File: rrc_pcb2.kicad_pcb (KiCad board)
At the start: 2 copper layers, 146.1 x 72.1 mm, 16 parts, among them J1 buzzer_toggle_pin, J2 battery_header, U1 BN220-GPS, U2 INA260, U3 Teensy4.1, U4 voltReg, U5 MS5611, U6 logo

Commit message: updated rrc_pcb2 schematic and pcb files
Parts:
- removed D1: ASMB-MTB0-0A3A2, LED_4pin:LED_4PIN
- J2: footprint Connector_JST:JST_GH_SM02B-GHS-TB_1x02-1MP_P1.25mm_Horizontal -> Connector_PinSocket_2.54mm:PinSocket_1x02_P2.54mm_Vertical
- turned J2 to 180 degrees
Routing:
- net B: track 10.1 -> 0.00 mm
- net G: track 7.12 -> 0.00 mm
- net R: track 7.12 -> 0.00 mm
- net Net-(J2-Pin_1): track 19.2 -> 16.3 mm
- net Net-(J2-Pin_2): track 18.8 -> 16.1 mm

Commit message: big cleanup of files
also new teensy4.1 symbo(the accurate one now) and fixed rfd900 schematic
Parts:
- J2: footprint Connector_PinSocket_2.54mm:PinSocket_1x02_P2.54mm_Vertical -> Connector_JST:JST_GH_SM02B-GHS-TB_1x02-1MP_P1.25mm_Horizontal
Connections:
- RF1 pad +5V: VCC -> (no net)
- RF1 pad GND: GND -> (no net)
- RF1 pad SIRX: RX2 -> (no net)
- RF1 pad SITX: TX2 -> (no net)
- U3 pad 0: (no net) -> unconnected-(U3-0_RX1_CRX2_CS1-Pad0)
- U3 pad 10: TX2 -> unconnected-(U3-10_CS_MQSR-Pad10)
- U3 pad 15: T_VCC -> unconnected-(U3-15_A1_RX3_SPDIF_IN-Pad15)
- U3 pad 16: SCL2 -> SCL1
- U3 pad 17: SDA2 -> SDA1
- U3 pad 18: Net-(BZ1--) -> SDA
- U3 pad 19: Net-(J1-Pin_2) -> SCL
- U3 pad 2: unconnected-(U3-0_RX1_CRX2_CS1-Pad2) -> B
- U3 pad 20: RX7 -> unconnected-(U3-20_A6_TX5_LRCLK1-Pad20)
- U3 pad 21: TX7 -> unconnected-(U3-21_A7_RX5_BCLK1-Pad21)
- U3 pad 24: unconnected-(U3-32_OUT1B-Pad24) -> SCL2
- U3 pad 25: unconnected-(U3-33_MCLK2-Pad25) -> SDA2
- U3 pad 26: unconnected-(U3-34_RX8-Pad26) -> Net-(BZ1--)
- U3 pad 27: unconnected-(U3-35_TX8-Pad27) -> Net-(J1-Pin_2)
- U3 pad 28: unconnected-(U3-36_CS-Pad28) -> RX7
- U3 pad 29: unconnected-(U3-37_CS-Pad29) -> TX7
- U3 pad 3: unconnected-(U3-1_TX1_CTX2_MISO1-Pad3) -> G
- U3 pad 38: SCL1 -> unconnected-(U3-38_CS1_IN1-Pad38)
- U3 pad 39: SDA1 -> unconnected-(U3-39_MISO1_OUT1A-Pad39)
- U3 pad 4: B -> R
- U3 pad 40: SDA -> unconnected-(U3-40_A16-Pad40)
- U3 pad 41: SCL -> unconnected-(U3-41_A17-Pad41)
- U3 pad 49: unconnected-(U3-VUSB-Pad49) -> (no net)
- U3 pad 5: G -> unconnected-(U3-5_IN2-Pad5)
- U3 pad 6: R -> unconnected-(U3-6_OUT1D-Pad6)
- U3 pad 66: unconnected-(U3-D--Pad66) -> (no net)
- U3 pad 67: unconnected-(U3-D+-Pad67) -> (no net)
- U3 pad 7: unconnected-(U3-5_IN2-Pad7) -> RX2
- U3 pad 8: unconnected-(U3-6_OUT1D-Pad8) -> TX2
- U3 pad 9: RX2 -> unconnected-(U3-9_OUT1C-Pad9)
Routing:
- net unconnected-(U3-10_CS_MQSR-Pad10): track 0.00 -> 107.0 mm
- net TX2: track 107.0 -> 0.00 mm
- net unconnected-(U3-9_OUT1C-Pad9): track 0.00 -> 100.9 mm
- net RX2: track 100.9 -> 0.00 mm

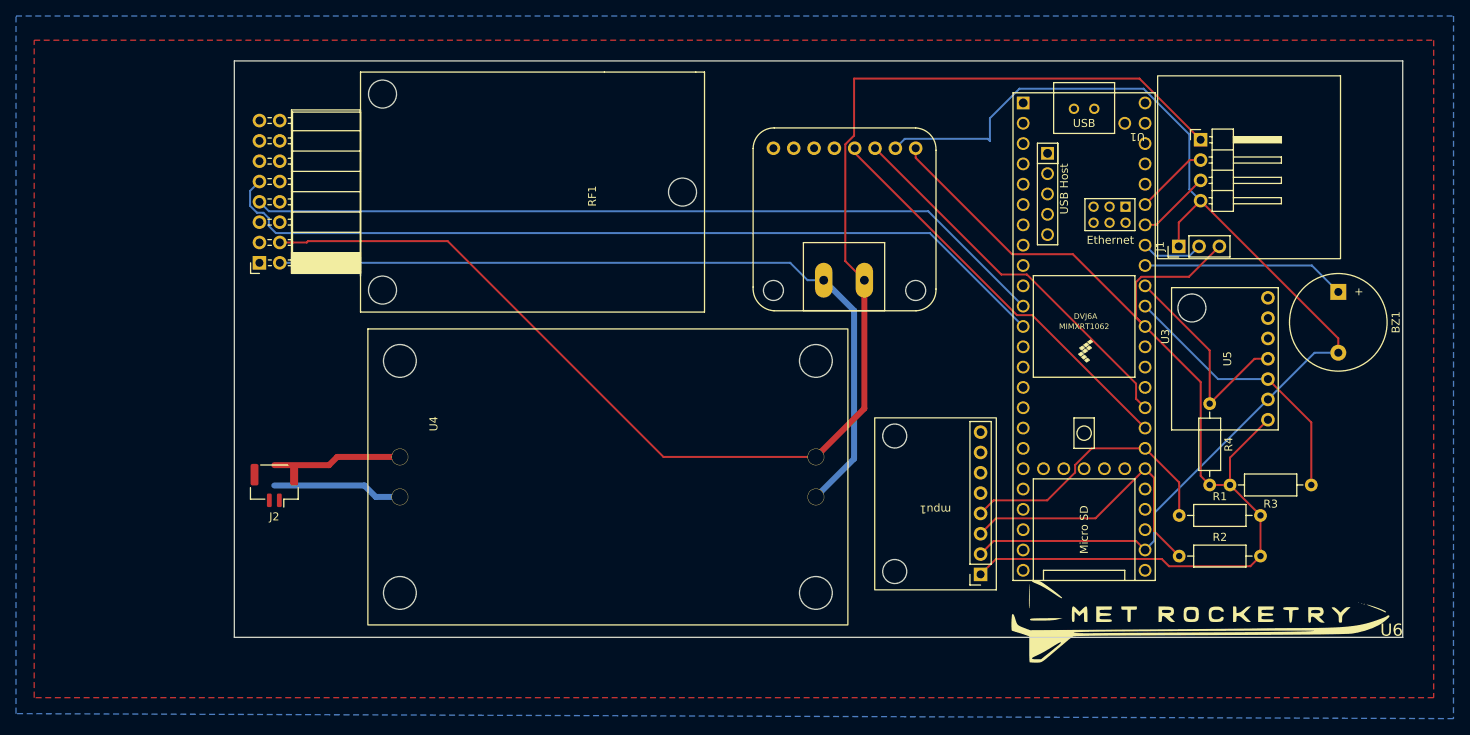
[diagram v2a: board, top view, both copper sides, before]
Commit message: fixed rfd and netlists for teensy4.1
fixed the rfd netlists and teensy pwr netlists and also fixed the pinout and wiring for rfd
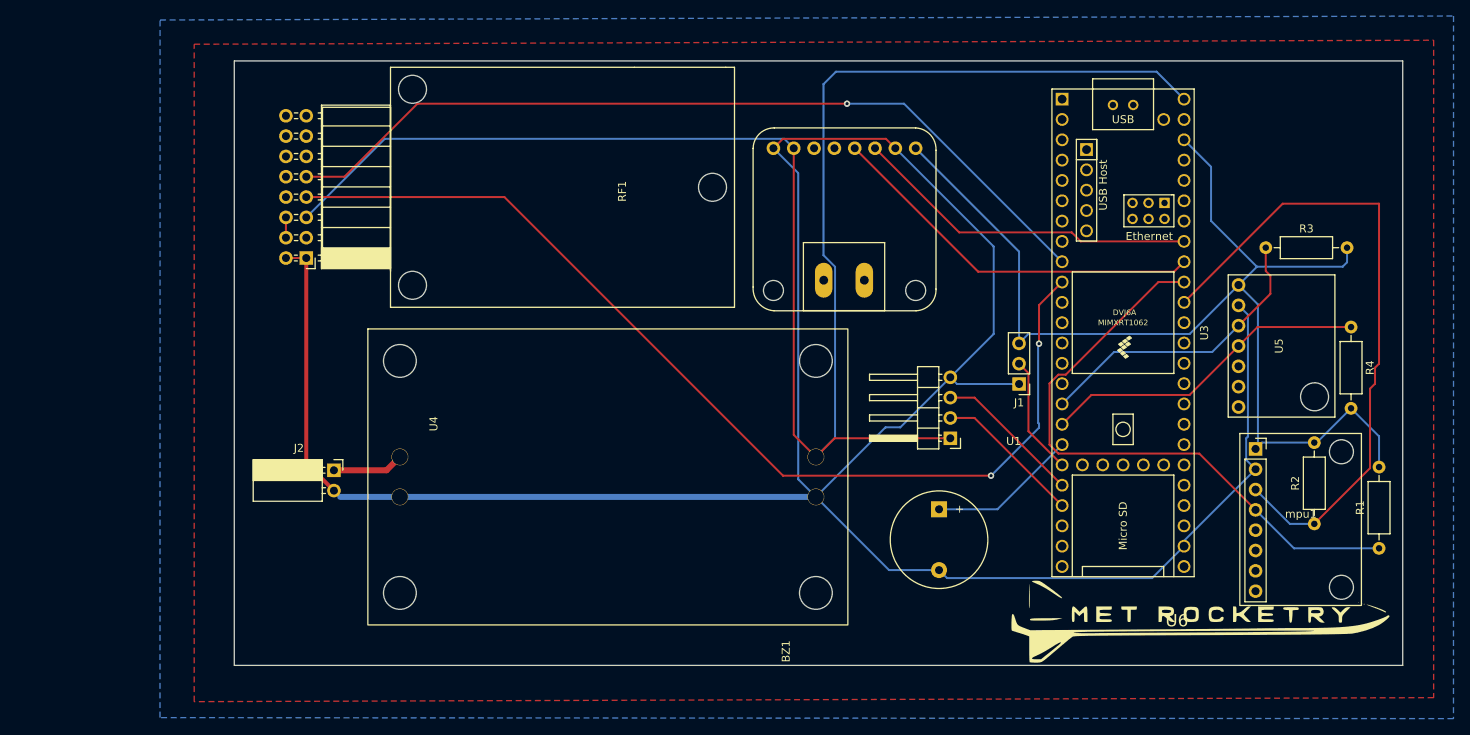
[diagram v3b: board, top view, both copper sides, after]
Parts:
- J2: footprint Connector_JST:JST_GH_SM02B-GHS-TB_1x02-1MP_P1.25mm_Horizontal -> Connector_PinSocket_2.54mm:PinSocket_1x02_P2.54mm_Horizontal
- moved U1 66.7 mm to (113.9, 53.0), turned to 0 degrees
- moved BZ1 56.8 mm to (130.0, 76.7)
- moved mpu1 45.7 mm to (175.2, 77.8), turned to 0 degrees
- moved R3 30.2 mm to (170.8, 44.0), turned to 0 degrees
- moved J1 26.4 mm to (140.0, 61.0), turned to 180 degrees
- moved R1 25.3 mm to (185.0, 81.6), turned to 90 degrees
- moved R4 20.1 mm to (181.5, 53.9)
- moved R2 17.4 mm to (176.9, 78.5), turned to 90 degrees
- moved U5 11.4 mm to (163.6, 56.3), turned to -90 degrees
- moved J2 7.69 mm to (54.4, 71.8), turned to 0 degrees
- moved U3 4.89 mm to (153.0, 54.6)
- moved RF1 3.80 mm to (61.4, 21.5)
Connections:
- BZ1 pad 2: T_GND -> GND
- J1 pad 1: T_GND -> GND
- J2 pad 2: Net-(J2-Pin_2) -> GND
- RF1 pad +5VUSB: (no net) -> VCC
- RF1 pad SIRX: (no net) -> TX2
- U1 pad 4: T_GND -> GND
- U2 pad 1: VCC -> unconnected-(U2-VIN+-Pad1)
- U2 pad 10: unconnected-(U2-IN--Pad10) -> GND
- U2 pad 2: GND -> unconnected-(U2-VIN--Pad2)
- U2 pad 4: T_GND -> GND
- U2 pad 9: unconnected-(U2-IN+-Pad9) -> VCC
- U3 pad 2: B -> unconnected-(U3-2_OUT2-Pad2)
- U3 pad 3: G -> unconnected-(U3-3_LRCLK2-Pad3)
- U3 pad 34: T_GND -> GND
- U3 pad 4: R -> unconnected-(U3-4_BCLK2-Pad4)
- U4 pad 2: Net-(J2-Pin_2) -> GND
- U5 pad 2: T_GND -> GND
- mpu1 pad 2: T_GND -> GND
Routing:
- net GND: track 99.5 -> 309.6 mm
- net T_GND: track 144.0 -> 0.00 mm
- net TX2: track 0.00 -> 128.3 mm, vias 0 -> 2
- net unconnected-(U3-10_CS_MQSR-Pad10): track 107.0 -> 0.00 mm
- net RX2: track 0.00 -> 106.4 mm, vias 0 -> 1
- net unconnected-(U3-9_OUT1C-Pad9): track 100.9 -> 0.00 mm
- net SCL1: track 36.6 -> 82.0 mm
- net VCC: track 176.0 -> 218.3 mm
- net SDA1: track 34.6 -> 76.3 mm
- net Net-(J2-Pin_2): track 16.1 -> 0.00 mm
- net SDA2: track 27.7 -> 41.2 mm
- net RX7: track 9.24 -> 18.5 mm
- net TX7: track 9.24 -> 18.5 mm
- net Net-(J2-Pin_1): track 16.3 -> 8.93 mm
- net Net-(J1-Pin_2): track 7.78 -> 14.9 mm
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- added copper zone on F.Cu, net (none)
- added copper zone on B.Cu, net GND
- removed copper zone on B.Cu, net T_GND
- removed copper zone on F.Cu, net T_VCC
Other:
- board size 146.1 x 72.1 mm -> 146.1 x 75.6 mm

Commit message: small fixes to traces
fixed pwr traces; moved them slightly away to avoid any possible bridging, also changed batt gnd to diff plate
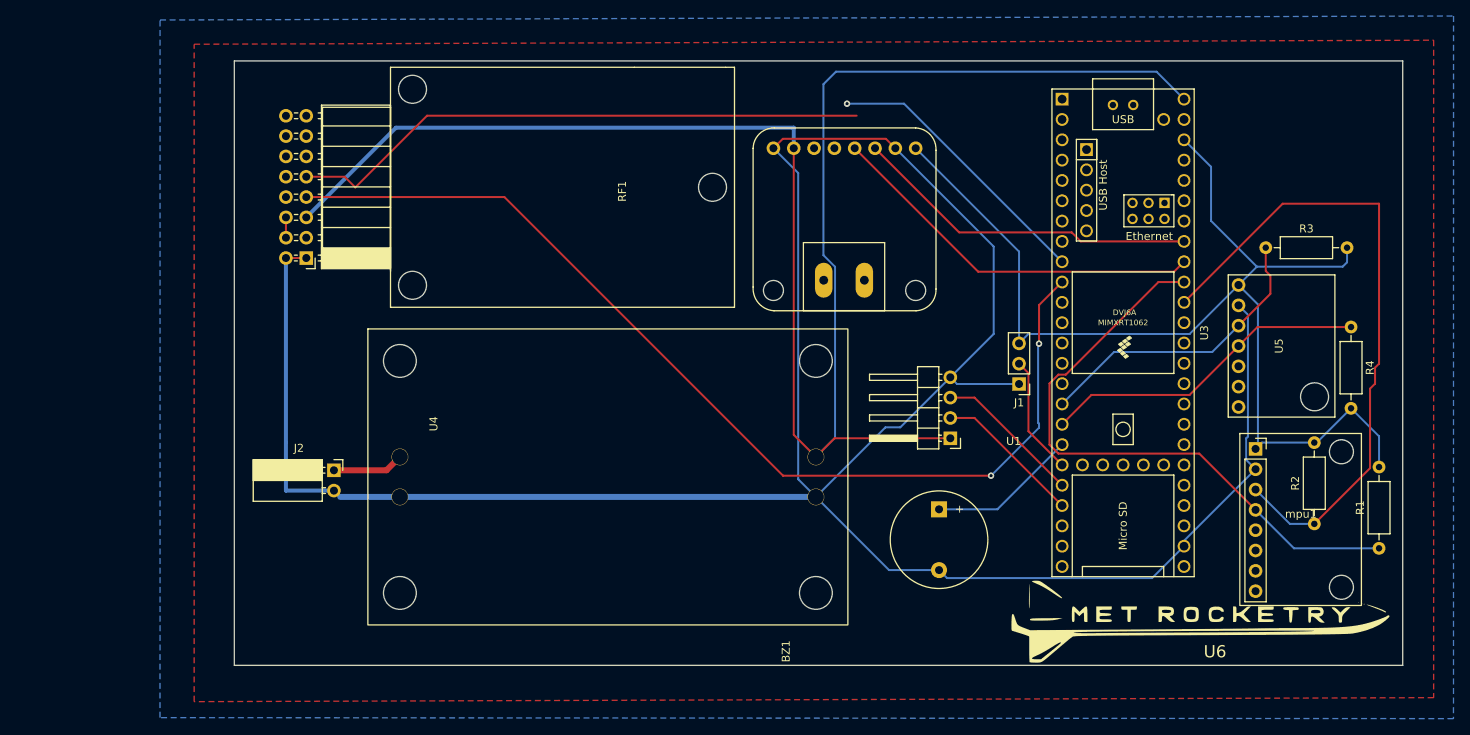
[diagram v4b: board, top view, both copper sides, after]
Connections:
- RF1 pad GND: (no net) -> GND
- U3 pad VIN: (no net) -> VCC
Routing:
- net GND: track 309.6 -> 314.2 mm
- net VCC: track 218.3 -> 221.0 mm
- net RX2: track 106.4 -> 108.1 mm
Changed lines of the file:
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@@
 			(layers "*.Cu" "*.Mask")
 			(remove_unused_layers no)
+			(net 2 "VCC")
 		)
 		(model "${KICAD_USER_DIR}/teensy.pretty/Teensy_4.1_Assembly.STEP"
@@
 		(at 159.724459 90.621103)
 		(property "Reference" "U6"
-			(at 0 0 0)
+			(at 4.775541 3.878897 0)
 			(layer "F.SilkS")
 			(effects
@@
 		(fp_arc
 			(start 11.351033 8.63642)
-			(mid 10.561541 10.466208)
+			(mid 10.56154 10.466212)
 			(end 8.709433 11.20182)
 			(stroke
@@
 			(layers "*.Cu" "*.Mask")
 			(remove_unused_layers no)
+			(net 1 "GND")
 		)
 		(pad "GND" thru_hole oval
@@
 			(layers "*.Cu" "*.Mask")
 			(remove_unused_layers no)
+			(net 1 "GND")
 		)
 		(pad "P0.1" thru_hole oval
@@
 	)
 	(segment
-		(start 50.901193 45.292707)
-		(end 50.901193 70.904861)
-		(width 0.5)
-		(layer "F.Cu")
-		(net 1)
-	)
-	(segment
 		(start 123.363834 30.392837)
 		(end 110.473834 30.392837)
@@
 	)
 	(segment
-		(start 50.901193 70.904861)
-		(end 54.360827 74.364495)
-		(width 0.5)
-		(layer "F.Cu")
-		(net 1)
-	)
-	(segment
 		(start 50.901193 45.292707)
 		(end 48.361193 45.292707)
@@
 	)
 	(segment
+		(start 48.361193 74.361193)
+		(end 48.364495 74.364495)
+		(width 0.25)
+		(layer "B.Cu")
+		(net 1)
+	)
+	(segment
 		(start 132.24857 61.04)
 		(end 131.410806 60.202236)
@@
 	)
 	(segment
+		(start 48.361193 45.292707)
+		(end 48.361193 68.364861)
+		(width 0.5)
+		(layer "B.Cu")
+		(net 1)
+	)
+	(segment
 		(start 130 84.3)
 		(end 131 85.3)
@@
 	)
 	(segment
+		(start 48.364495 74.364495)
+		(end 54.360827 74.364495)
+		(width 0.5)
+		(layer "B.Cu")
+		(net 1)
+	)
+	(segment
+		(start 48.361193 68.364861)
+		(end 48.361193 74.361193)
+		(width 0.5)
+		(layer "B.Cu")
+		(net 1)
+	)
+	(segment
 		(start 140 61.04)
 		(end 132.24857 61.04)
@@
 	)
 	(segment
-		(start 50.901193 40.212707)
-		(end 60.721063 30.392837)
-		(width 0.25)
-		(layer "B.Cu")
-		(net 2)
-	)
-	(segment
 		(start 160.62386 25.433432)
 		(end 157.190428 22)
@@
 	)
 	(segment
-		(start 110.663834 30.392837)
-		(end 111.838834 31.567837)
-		(width 0.25)
+		(start 55.80695 35.30695)
+		(end 62.1139 29)
+		(width 0.5)
 		(layer "B.Cu")
 		(net 2)
@@
 	)
 	(segment
+		(start 50.901193 40.212707)
+		(end 55.80695 35.30695)
+		(width 0.5)
+		(layer "B.Cu")
+		(net 2)
+	)
+	(segment
 		(start 157.190428 22)
 		(end 117.107668 22)
@@
 	)
 	(segment
-		(start 60.721063 30.392837)
-		(end 110.663834 30.392837)
-		(width 0.25)
+		(start 111.838834 29)
+		(end 111.838834 31.567837)
+		(width 0.5)
 		(layer "B.Cu")
 		(net 2)
@@
 	)
 	(segment
+		(start 62.1139 29)
+		(end 111.838834 29)
+		(width 0.5)
+		(layer "B.Cu")
+		(net 2)
+	)
+	(segment
 		(start 183.875 61.625)
 		(end 183.875 71.555786)
@@
 	)
 	(segment
-		(start 55.67105 35.132707)
-		(end 50.901193 35.132707)
+		(start 119.696243 27.5)
+		(end 66 27.5)
+		(width 0.25)
+		(layer "F.Cu")
+		(net 55)
+	)
+	(segment
+		(start 50.901193 35.132707)
+		(end 55.69606 35.132707)
 		(width 0.25)
 		(layer "F.Cu")
@@
 	)
 	(segment
-		(start 118.5 26)
-		(end 64.803757 26)
+		(start 55.69606 35.132707)
+		(end 57.031677 36.468324)
 		(width 0.25)
 		(layer "F.Cu")
@@
 	)
 	(segment
-		(start 64.803757 26)
-		(end 55.67105 35.132707)
+		(start 66 27.5)
+		(end 57.031677 36.468324)
 		(width 0.25)
 		(layer "F.Cu")
@@
 		(min_thickness 0.254)
 		(filled_areas_thickness no)
-		(fill
+		(fill yes
 			(thermal_gap 0.508)
 			(thermal_bridge_width 0.508)
@@
 		(min_thickness 0.254)
 		(filled_areas_thickness no)
-		(fill
+		(fill yes
 			(thermal_gap 0.508)
 			(thermal_bridge_width 0.508)

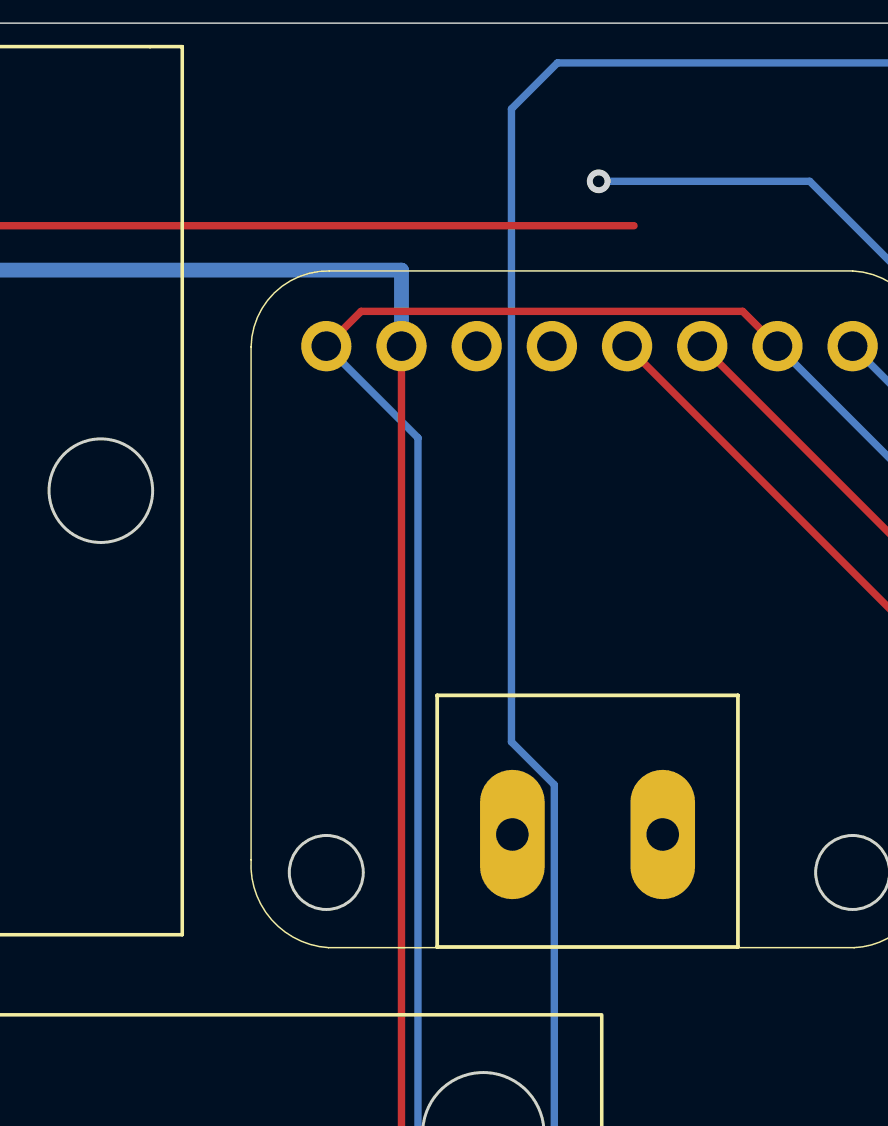
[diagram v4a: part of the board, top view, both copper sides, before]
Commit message: exported pcb to fabrication
also fixed rfd rx trace
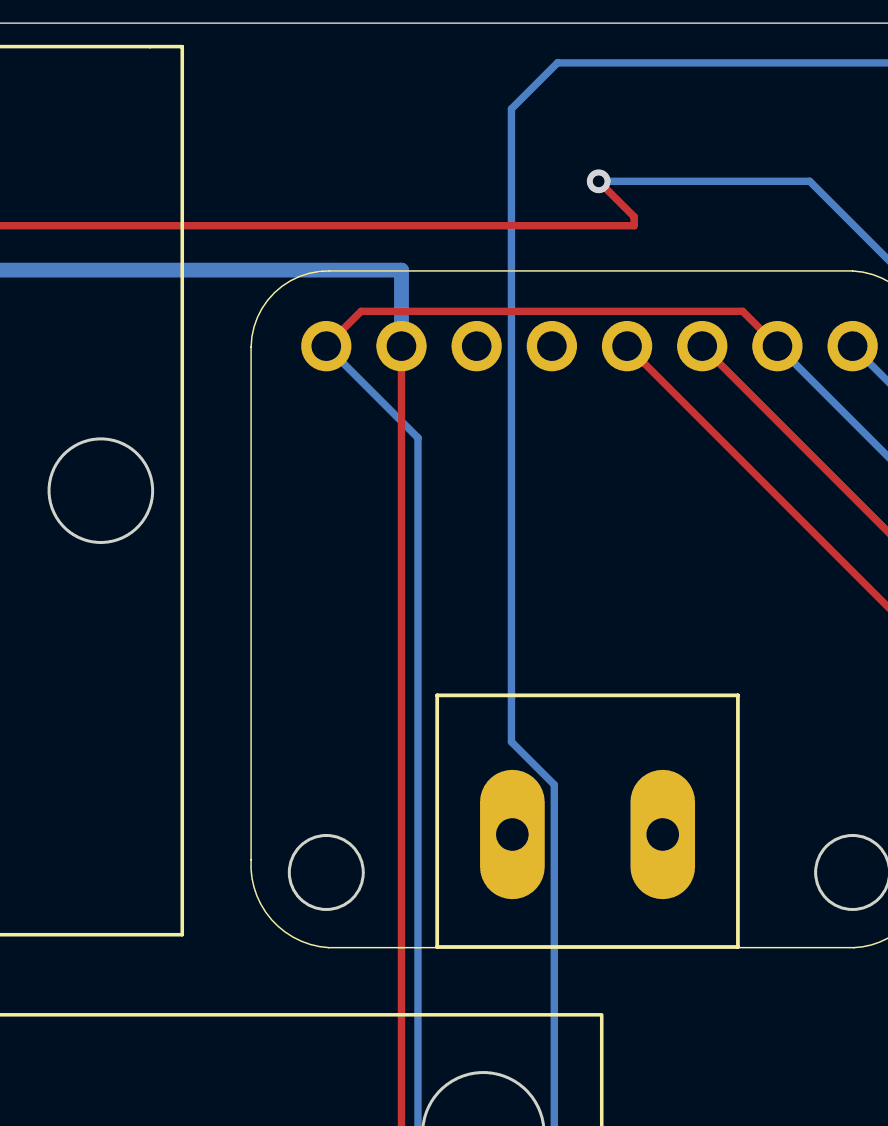
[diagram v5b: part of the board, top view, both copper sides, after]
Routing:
- net RX2: track 108.1 -> 110.1 mm
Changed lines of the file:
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@@
 		(fp_arc
 			(start 11.351033 8.63642)
-			(mid 10.56154 10.466212)
+			(mid 10.561542 10.466212)
 			(end 8.709433 11.20182)
 			(stroke
@@
 		(fp_arc
 			(start 8.734833 -11.65818)
-			(mid 10.65842 -10.714117)
+			(mid 10.658416 -10.714117)
 			(end 11.351033 -8.68638)
 			(stroke
@@
 	)
 	(segment
+		(start 119.696243 27.5)
+		(end 119.696243 27.196243)
+		(width 0.25)
+		(layer "F.Cu")
+		(net 55)
+	)
+	(segment
 		(start 50.901193 35.132707)
 		(end 55.69606 35.132707)
@@
 		(width 0.25)
 		(layer "F.Cu")
+		(net 55)
+	)
+	(segment
+		(start 119.696243 27.196243)
+		(end 118.5 26)
+		(width 0.25)
+		(layer "F.Cu")
